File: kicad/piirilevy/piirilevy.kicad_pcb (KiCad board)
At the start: 2 copper layers, 54.6 x 100.3 mm, 88 parts, among them J1 AVR-ISP, SW1 SW_SPST, SW2 SW_Push, SW3 SW_Push, SW4 SW_Push, U1 LM324, U2 LM7805CV, U3 ATmega328P, U4 MAX5033B, U5 MCP3202, U6 47C16, Y1 16MHz

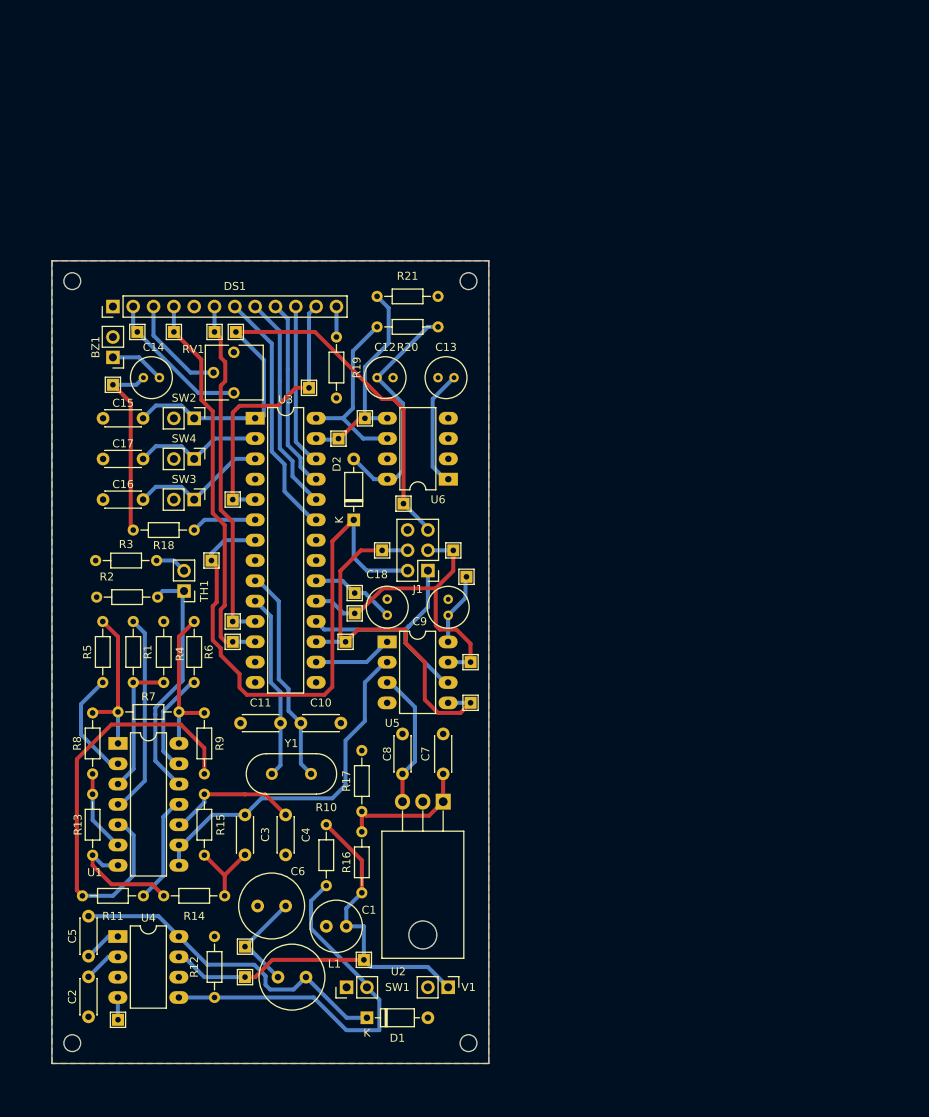
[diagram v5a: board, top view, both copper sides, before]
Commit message: Yksipuoleinen piirilevy.
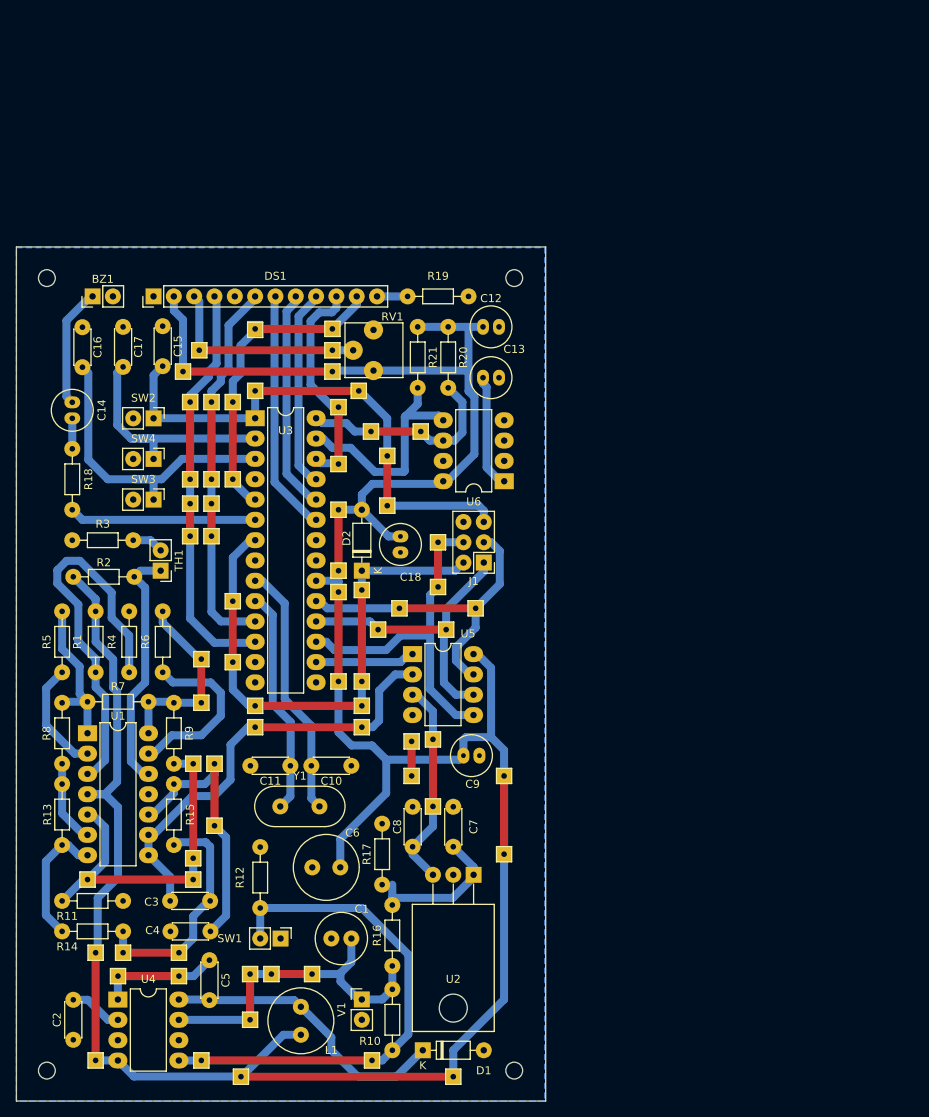
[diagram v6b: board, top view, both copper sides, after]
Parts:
- removed the REF** at (119.4, 83.8)
- removed the REF** at (105.0, 69.8)
- removed the REF** at (121.5, 97.8)
- removed the REF** at (108.3, 67.3)
- removed the REF** at (107.1, 91.7)
- removed the REF** at (92.2, 56.5)
- removed the REF** at (101.3, 63.5)
- removed the REF** at (110.5, 83.8)
- removed the REF** at (105.9, 95.2)
- removed the REF** at (77.5, 142.5)
- removed the REF** at (121.5, 102.9)
- removed the REF** at (76.8, 63.1)
- removed the REF** at (91.8, 95.2)
- removed the REF** at (108.2, 135.0)
- removed the REF** at (79.9, 56.5)
- removed the REF** at (84.5, 56.5)
- removed the REF** at (93.3, 133.3)
- removed the REF** at (89.2, 85.1)
- removed the REF** at (91.8, 77.5)
- removed the REF** at (91.8, 92.7)
- removed the REF** at (93.3, 137.2)
- removed the REF** at (121.0, 87.1)
- removed the REF** at (89.5, 56.5)
- removed the REF** at (113.2, 78.0)
- removed the REF** at (107.1, 89.2)
- added REF**: TestPoint_THTPad_1.5x1.5mm_Drill0.7mm, TestPoint:TestPoint_THTPad_1.5x1.5mm_Drill0.7mm, F.Cu at (108.0, 88.8)
- added REF**: TestPoint_THTPad_1.5x1.5mm_Drill0.7mm, TestPoint:TestPoint_THTPad_1.5x1.5mm_Drill0.7mm, F.Cu at (87.6, 58.8)
- added REF**: TestPoint_THTPad_1.5x1.5mm_Drill0.7mm, TestPoint:TestPoint_THTPad_1.5x1.5mm_Drill0.7mm, F.Cu at (111.1, 78.2)
- added REF**: TestPoint_THTPad_1.5x1.5mm_Drill0.7mm, TestPoint:TestPoint_THTPad_1.5x1.5mm_Drill0.7mm, F.Cu at (86.9, 110.5)
- added REF**: TestPoint_THTPad_1.5x1.5mm_Drill0.7mm, TestPoint:TestPoint_THTPad_1.5x1.5mm_Drill0.7mm, F.Cu at (114.2, 107.7)
- added REF**: TestPoint_THTPad_1.5x1.5mm_Drill0.7mm, TestPoint:TestPoint_THTPad_1.5x1.5mm_Drill0.7mm, F.Cu at (89.2, 74.9)
- added REF**: TestPoint_THTPad_1.5x1.5mm_Drill0.7mm, TestPoint:TestPoint_THTPad_1.5x1.5mm_Drill0.7mm, F.Cu at (86.9, 122.3)
- added REF**: TestPoint_THTPad_1.5x1.5mm_Drill0.7mm, TestPoint:TestPoint_THTPad_1.5x1.5mm_Drill0.7mm, F.Cu at (86.5, 78.0)
- added REF**: TestPoint_THTPad_1.5x1.5mm_Drill0.7mm, TestPoint:TestPoint_THTPad_1.5x1.5mm_Drill0.7mm, F.Cu at (87.9, 147.6)
- added REF**: TestPoint_THTPad_1.5x1.5mm_Drill0.7mm, TestPoint:TestPoint_THTPad_1.5x1.5mm_Drill0.7mm, F.Cu at (94.6, 105.9)
- added REF**: TestPoint_THTPad_1.5x1.5mm_Drill0.7mm, TestPoint:TestPoint_THTPad_1.5x1.5mm_Drill0.7mm, F.Cu at (105.0, 86.4)
- added REF**: TestPoint_THTPad_1.5x1.5mm_Drill0.7mm, TestPoint:TestPoint_THTPad_1.5x1.5mm_Drill0.7mm, F.Cu at (105.0, 100.2)
- added REF**: TestPoint_THTPad_1.5x1.5mm_Drill0.7mm, TestPoint:TestPoint_THTPad_1.5x1.5mm_Drill0.7mm, F.Cu at (101.7, 136.8)
- added REF**: TestPoint_THTPad_1.5x1.5mm_Drill0.7mm, TestPoint:TestPoint_THTPad_1.5x1.5mm_Drill0.7mm, F.Cu at (89.5, 118.2)
- added REF**: TestPoint_THTPad_1.5x1.5mm_Drill0.7mm, TestPoint:TestPoint_THTPad_1.5x1.5mm_Drill0.7mm, F.Cu at (89.2, 82.0)
- added REF**: TestPoint_THTPad_1.5x1.5mm_Drill0.7mm, TestPoint:TestPoint_THTPad_1.5x1.5mm_Drill0.7mm, F.Cu at (92.8, 149.6)
- added REF**: TestPoint_THTPad_1.5x1.5mm_Drill0.7mm, TestPoint:TestPoint_THTPad_1.5x1.5mm_Drill0.7mm, F.Cu at (91.8, 97.8)
- added REF**: TestPoint_THTPad_1.5x1.5mm_Drill0.7mm, TestPoint:TestPoint_THTPad_1.5x1.5mm_Drill0.7mm, F.Cu at (111.1, 72.0)
- added REF**: TestPoint_THTPad_1.5x1.5mm_Drill0.7mm, TestPoint:TestPoint_THTPad_1.5x1.5mm_Drill0.7mm, F.Cu at (85.1, 134.1)
- added REF**: TestPoint_THTPad_1.5x1.5mm_Drill0.7mm, TestPoint:TestPoint_THTPad_1.5x1.5mm_Drill0.7mm, F.Cu at (87.9, 102.9)
- added REF**: TestPoint_THTPad_1.5x1.5mm_Drill0.7mm, TestPoint:TestPoint_THTPad_1.5x1.5mm_Drill0.7mm, F.Cu at (117.5, 88.4)
- added REF**: TestPoint_THTPad_1.5x1.5mm_Drill0.7mm, TestPoint:TestPoint_THTPad_1.5x1.5mm_Drill0.7mm, F.Cu at (107.6, 63.9)
- added REF**: TestPoint_THTPad_1.5x1.5mm_Drill0.7mm, TestPoint:TestPoint_THTPad_1.5x1.5mm_Drill0.7mm, F.Cu at (108.0, 105.9)
- added REF**: TestPoint_THTPad_1.5x1.5mm_Drill0.7mm, TestPoint:TestPoint_THTPad_1.5x1.5mm_Drill0.7mm, F.Cu at (94.6, 103.3)
- added REF**: TestPoint_THTPad_1.5x1.5mm_Drill0.7mm, TestPoint:TestPoint_THTPad_1.5x1.5mm_Drill0.7mm, F.Cu at (115.3, 69.0)
- added REF**: TestPoint_THTPad_1.5x1.5mm_Drill0.7mm, TestPoint:TestPoint_THTPad_1.5x1.5mm_Drill0.7mm, F.Cu at (104.3, 58.8)
- added REF**: TestPoint_THTPad_1.5x1.5mm_Drill0.7mm, TestPoint:TestPoint_THTPad_1.5x1.5mm_Drill0.7mm, F.Cu at (91.8, 65.3)
- added REF**: TestPoint_THTPad_1.5x1.5mm_Drill0.7mm, TestPoint:TestPoint_THTPad_1.5x1.5mm_Drill0.7mm, F.Cu at (89.2, 65.3)
- added REF**: TestPoint_THTPad_1.5x1.5mm_Drill0.7mm, TestPoint:TestPoint_THTPad_1.5x1.5mm_Drill0.7mm, F.Cu at (85.1, 137.0)
- added REF**: TestPoint_THTPad_1.5x1.5mm_Drill0.7mm, TestPoint:TestPoint_THTPad_1.5x1.5mm_Drill0.7mm, F.Cu at (105.0, 73.0)
- added REF**: TestPoint_THTPad_1.5x1.5mm_Drill0.7mm, TestPoint:TestPoint_THTPad_1.5x1.5mm_Drill0.7mm, F.Cu at (110.0, 93.7)
- added REF**: TestPoint_THTPad_1.5x1.5mm_Drill0.7mm, TestPoint:TestPoint_THTPad_1.5x1.5mm_Drill0.7mm, F.Cu at (86.5, 74.9)
- added REF**: TestPoint_THTPad_1.5x1.5mm_Drill0.7mm, TestPoint:TestPoint_THTPad_1.5x1.5mm_Drill0.7mm, F.Cu at (119.4, 149.6)
- added REF**: TestPoint_THTPad_1.5x1.5mm_Drill0.7mm, TestPoint:TestPoint_THTPad_1.5x1.5mm_Drill0.7mm, F.Cu at (94.0, 142.5)
- added REF**: TestPoint_THTPad_1.5x1.5mm_Drill0.7mm, TestPoint:TestPoint_THTPad_1.5x1.5mm_Drill0.7mm, F.Cu at (89.5, 110.5)
- added REF**: TestPoint_THTPad_1.5x1.5mm_Drill0.7mm, TestPoint:TestPoint_THTPad_1.5x1.5mm_Drill0.7mm, F.Cu at (108.0, 100.2)
- added REF**: TestPoint_THTPad_1.5x1.5mm_Drill0.7mm, TestPoint:TestPoint_THTPad_1.5x1.5mm_Drill0.7mm, F.Cu at (105.0, 78.7)
- added REF**: TestPoint_THTPad_1.5x1.5mm_Drill0.7mm, TestPoint:TestPoint_THTPad_1.5x1.5mm_Drill0.7mm, F.Cu at (104.3, 61.5)
- added REF**: TestPoint_THTPad_1.5x1.5mm_Drill0.7mm, TestPoint:TestPoint_THTPad_1.5x1.5mm_Drill0.7mm, F.Cu at (86.5, 65.3)
- added REF**: TestPoint_THTPad_1.5x1.5mm_Drill0.7mm, TestPoint:TestPoint_THTPad_1.5x1.5mm_Drill0.7mm, F.Cu at (125.7, 121.8)
- added REF**: TestPoint_THTPad_1.5x1.5mm_Drill0.7mm, TestPoint:TestPoint_THTPad_1.5x1.5mm_Drill0.7mm, F.Cu at (118.5, 93.7)
- added REF**: TestPoint_THTPad_1.5x1.5mm_Drill0.7mm, TestPoint:TestPoint_THTPad_1.5x1.5mm_Drill0.7mm, F.Cu at (114.2, 112.0)
- added REF**: TestPoint_THTPad_1.5x1.5mm_Drill0.7mm, TestPoint:TestPoint_THTPad_1.5x1.5mm_Drill0.7mm, F.Cu at (78.1, 134.1)
- added REF**: TestPoint_THTPad_1.5x1.5mm_Drill0.7mm, TestPoint:TestPoint_THTPad_1.5x1.5mm_Drill0.7mm, F.Cu at (94.6, 56.3)
- added REF**: TestPoint_THTPad_1.5x1.5mm_Drill0.7mm, TestPoint:TestPoint_THTPad_1.5x1.5mm_Drill0.7mm, F.Cu at (86.5, 82.0)
- added REF**: TestPoint_THTPad_1.5x1.5mm_Drill0.7mm, TestPoint:TestPoint_THTPad_1.5x1.5mm_Drill0.7mm, F.Cu at (105.0, 65.9)
- added REF**: TestPoint_THTPad_1.5x1.5mm_Drill0.7mm, TestPoint:TestPoint_THTPad_1.5x1.5mm_Drill0.7mm, F.Cu at (109.1, 69.0)
- added REF**: TestPoint_THTPad_1.5x1.5mm_Drill0.7mm, TestPoint:TestPoint_THTPad_1.5x1.5mm_Drill0.7mm, F.Cu at (91.8, 90.2)
- added REF**: TestPoint_THTPad_1.5x1.5mm_Drill0.7mm, TestPoint:TestPoint_THTPad_1.5x1.5mm_Drill0.7mm, F.Cu at (74.7, 147.6)
- added REF**: TestPoint_THTPad_1.5x1.5mm_Drill0.7mm, TestPoint:TestPoint_THTPad_1.5x1.5mm_Drill0.7mm, F.Cu at (94.0, 136.8)
- added REF**: TestPoint_THTPad_1.5x1.5mm_Drill0.7mm, TestPoint:TestPoint_THTPad_1.5x1.5mm_Drill0.7mm, F.Cu at (108.0, 103.3)
- added REF**: TestPoint_THTPad_1.5x1.5mm_Drill0.7mm, TestPoint:TestPoint_THTPad_1.5x1.5mm_Drill0.7mm, F.Cu at (116.8, 107.4)
- added REF**: TestPoint_THTPad_1.5x1.5mm_Drill0.7mm, TestPoint:TestPoint_THTPad_1.5x1.5mm_Drill0.7mm, F.Cu at (125.7, 112.0)
- added REF**: TestPoint_THTPad_1.5x1.5mm_Drill0.7mm, TestPoint:TestPoint_THTPad_1.5x1.5mm_Drill0.7mm, F.Cu at (77.5, 137.0)
- added REF**: TestPoint_THTPad_1.5x1.5mm_Drill0.7mm, TestPoint:TestPoint_THTPad_1.5x1.5mm_Drill0.7mm, F.Cu at (94.6, 63.9)
- added REF**: TestPoint_THTPad_1.5x1.5mm_Drill0.7mm, TestPoint:TestPoint_THTPad_1.5x1.5mm_Drill0.7mm, F.Cu at (96.6, 136.8)
- added REF**: TestPoint_THTPad_1.5x1.5mm_Drill0.7mm, TestPoint:TestPoint_THTPad_1.5x1.5mm_Drill0.7mm, F.Cu at (87.9, 97.4)
- added REF**: TestPoint_THTPad_1.5x1.5mm_Drill0.7mm, TestPoint:TestPoint_THTPad_1.5x1.5mm_Drill0.7mm, F.Cu at (74.7, 134.1)
- added REF**: TestPoint_THTPad_1.5x1.5mm_Drill0.7mm, TestPoint:TestPoint_THTPad_1.5x1.5mm_Drill0.7mm, F.Cu at (109.2, 147.6)
- added REF**: TestPoint_THTPad_1.5x1.5mm_Drill0.7mm, TestPoint:TestPoint_THTPad_1.5x1.5mm_Drill0.7mm, F.Cu at (122.2, 91.1)
- added REF**: TestPoint_THTPad_1.5x1.5mm_Drill0.7mm, TestPoint:TestPoint_THTPad_1.5x1.5mm_Drill0.7mm, F.Cu at (85.6, 61.5)
- added REF**: TestPoint_THTPad_1.5x1.5mm_Drill0.7mm, TestPoint:TestPoint_THTPad_1.5x1.5mm_Drill0.7mm, F.Cu at (73.7, 125.0)
- added REF**: TestPoint_THTPad_1.5x1.5mm_Drill0.7mm, TestPoint:TestPoint_THTPad_1.5x1.5mm_Drill0.7mm, F.Cu at (105.0, 89.0)
- added REF**: TestPoint_THTPad_1.5x1.5mm_Drill0.7mm, TestPoint:TestPoint_THTPad_1.5x1.5mm_Drill0.7mm, F.Cu at (91.8, 74.9)
- added REF**: TestPoint_THTPad_1.5x1.5mm_Drill0.7mm, TestPoint:TestPoint_THTPad_1.5x1.5mm_Drill0.7mm, F.Cu at (117.5, 82.8)
- added REF**: TestPoint_THTPad_1.5x1.5mm_Drill0.7mm, TestPoint:TestPoint_THTPad_1.5x1.5mm_Drill0.7mm, F.Cu at (116.8, 115.8)
- added REF**: TestPoint_THTPad_1.5x1.5mm_Drill0.7mm, TestPoint:TestPoint_THTPad_1.5x1.5mm_Drill0.7mm, F.Cu at (104.3, 56.1)
- added REF**: TestPoint_THTPad_1.5x1.5mm_Drill0.7mm, TestPoint:TestPoint_THTPad_1.5x1.5mm_Drill0.7mm, F.Cu at (112.6, 91.1)
- added REF**: TestPoint_THTPad_1.5x1.5mm_Drill0.7mm, TestPoint:TestPoint_THTPad_1.5x1.5mm_Drill0.7mm, F.Cu at (86.9, 125.0)
- added REF**: TestPoint_THTPad_1.5x1.5mm_Drill0.7mm, TestPoint:TestPoint_THTPad_1.5x1.5mm_Drill0.7mm, F.Cu at (89.2, 78.0)
- moved H3 55.4 mm to (127.0, 148.8)
- moved H1 52.8 mm to (68.6, 148.8)
- moved R10 22.2 mm to (111.8, 138.7)
- moved C16 21.7 mm to (73.0, 55.9), turned to -90 degrees
- moved R19 20.8 mm to (121.3, 52.1), turned to 180 degrees
- moved C5 18.4 mm to (88.9, 140.0), turned to 90 degrees
- moved RV1 17.7 mm to (109.4, 56.3)
- moved C9 17.6 mm to (120.7, 109.5), turned to 0 degrees
- moved C4 17.3 mm to (89.0, 131.4), turned to 180 degrees
- moved C17 16.7 mm to (78.1, 55.9), turned to -90 degrees
- moved C12 16.5 mm to (125.1, 55.9), turned to 180 degrees
- moved R18 15.5 mm to (71.8, 78.7), turned to 90 degrees
- moved C15 13.7 mm to (83.1, 55.8), turned to -90 degrees
- moved R14 13.5 mm to (70.5, 131.4)
- moved R12 12.6 mm to (95.2, 128.5)
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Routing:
- net VCC: track 110.1 -> 347.6 mm
- net Net-(R1-Pad1): track 17.4 -> 48.9 mm
- net SW_2: track 17.4 -> 39.6 mm
- net Net-(C3-Pad1): track 9.76 -> 29.5 mm
- net Net-(C14-Pad1): track 23.4 -> 3.81 mm
- net Net-(C4-Pad1): track 16.6 -> 34.7 mm
- net V_KÄYTTÖ: track 58.8 -> 42.8 mm
- net Net-(R10-Pad2): track 49.1 -> 64.7 mm
- net BUZZER: track 8.15 -> 23.4 mm
- net SW_1: track 16.4 -> 29.7 mm
- net Net-(DS1-Pad3): track 13.0 -> 26.2 mm
- net VAHVISTIN_LÄHTÖ: track 44.1 -> 55.4 mm
- net Net-(C5-Pad2): track 4.68 -> 15.2 mm
- net Net-(R11-Pad2): track 54.5 -> 44.7 mm
- net Net-(R6-Pad1): track 13.0 -> 22.2 mm
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- removed copper zone on F.Cu, net VCC
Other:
- board size 54.6 x 100.3 mm -> 66.2 x 106.8 mm

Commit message: ...
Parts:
- removed the REF** at (89.2, 74.9)
- removed the REF** at (86.5, 78.0)
- removed the REF** at (86.5, 74.9)
- removed the REF** at (89.2, 78.0)
- moved REF** 0.38 mm to (87.9, 97.8)
